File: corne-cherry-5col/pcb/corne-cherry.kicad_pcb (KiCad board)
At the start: 2 copper layers, 237.5 x 105.6 mm, 152 parts, among them J1 MJ-4PP-9, J2 OLED, J3 MJ-4PP-9, J4 OLED, SW10 SW_PUSH, SW11 SW_PUSH, SW12 SW_PUSH, SW14 SW_PUSH, SW15 SW_PUSH, SW16 SW_PUSH, SW17 SW_PUSH, SW18 SW_PUSH, SW19 SW_PUSH, SW2 SW_PUSH, SW20 SW_PUSH, SW21 SW_PUSH, SW23 SW_PUSH, SW24 SW_PUSH, SW25 SW_PUSH, SW26 SW_PUSH, SW27 SW_PUSH, SW29 SW_PUSH, SW3 SW_PUSH, SW30 SW_PUSH, SW31 SW_PUSH, SW32 SW_PUSH, SW33 SW_PUSH, SW35 SW_PUSH, SW36 SW_PUSH, SW37 SW_PUSH, SW38 SW_PUSH, SW39 SW_PUSH, SW4 SW_PUSH, SW40 SW_PUSH, SW41 SW_PUSH, SW42 SW_PUSH, SW5 SW_PUSH, SW6 SW_PUSH, SW8 SW_PUSH, SW9 SW_PUSH, U1 ProMicro, U2 ProMicro

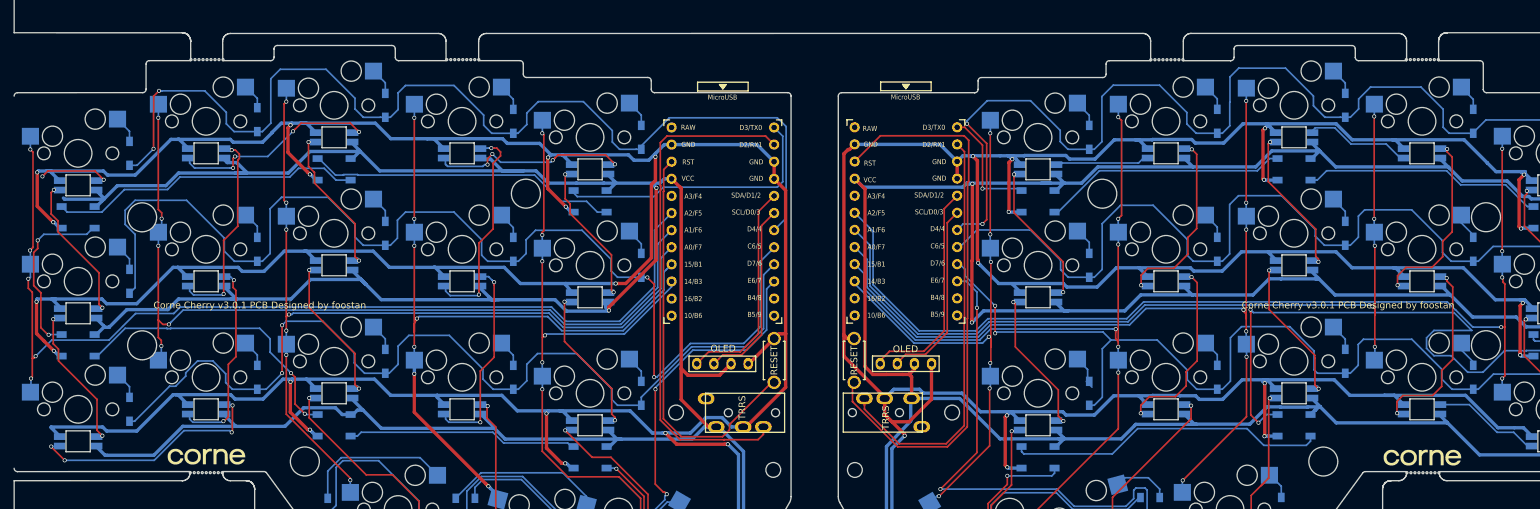
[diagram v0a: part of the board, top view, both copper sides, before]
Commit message: minor fixes to 5col
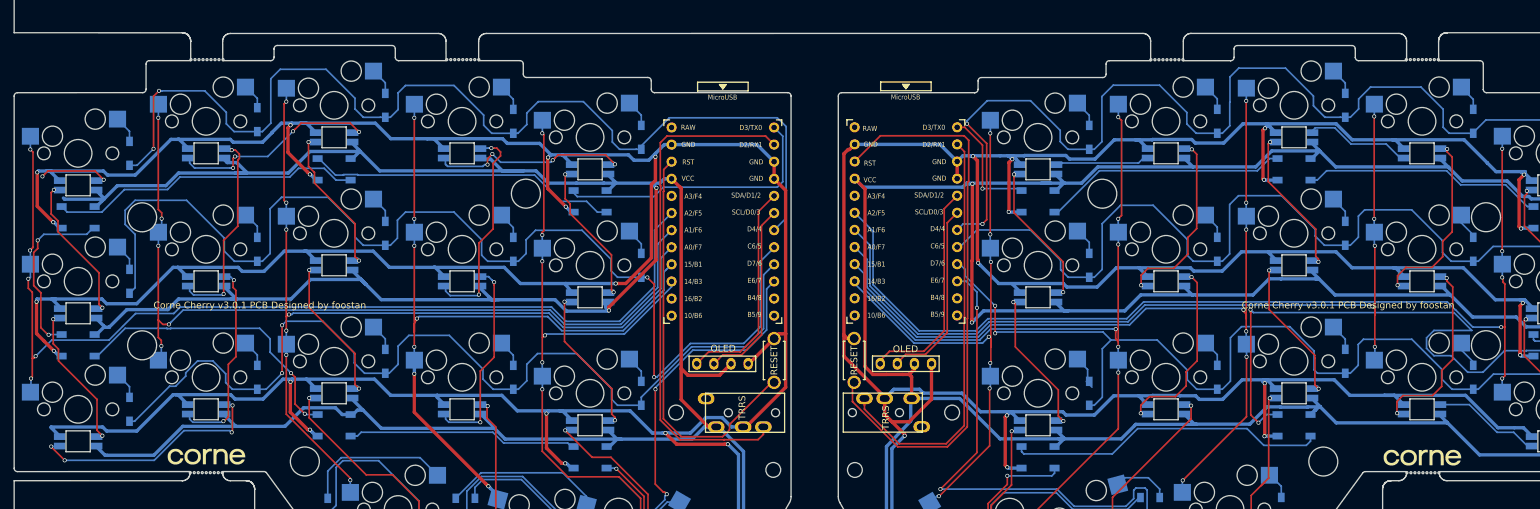
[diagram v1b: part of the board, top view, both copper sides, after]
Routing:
- net col1_r: track 151.9 -> 150.1 mm
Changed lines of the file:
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@@
   (gr_line (start 55.7125 83.245) (end 55.7175 83.020309)
     (stroke (width 0.2) (type solid)) (layer "Edge.Cuts"))
-  (gr_line (start 93.7275 22.020252) (end 93.7125 19.1227)
-    (stroke (width 0.2) (type solid)) (layer "Edge.Cuts"))
   (gr_line (start 93.7125 19.1227) (end 93.7125 19.1169)
     (stroke (width 0.2) (type solid)) (layer "Edge.Cuts"))
@@
   (gr_line (start 67.688301 22.018729) (end 60.5775 22.018729)
     (stroke (width 0.2) (type solid)) (layer "Edge.Cuts"))
-  (gr_line (start 49.189499 22.519109) (end 49.189499 26.268145)
-    (stroke (width 0.2) (type solid)) (layer "Edge.Cuts"))
   (gr_curve (pts (xy 124.190287 25.020242) (xy 124.190346 24.744107) (xy 123.966569 24.520195) (xy 123.690423 24.520121))
     (stroke (width 0.2) (type solid)) (layer "Edge.Cuts"))
@@
   (gr_line (start 104.688444 22.018729) (end 98.5675 22.018729)
     (stroke (width 0.2) (type solid)) (layer "Edge.Cuts"))
-  (gr_line (start 86.189642 21.51835) (end 86.189642 20.268671)
-    (stroke (width 0.2) (type solid)) (layer "Edge.Cuts"))
-  (gr_line (start 85.689263 19.768292) (end 68.68906 19.768292)
-    (stroke (width 0.2) (type solid)) (layer "Edge.Cuts"))
   (gr_line (start 144.939784 27.268904) (end 144.939784 86.742945)
     (stroke (width 0.2) (type solid)) (layer "Edge.Cuts"))
@@
   (gr_line (start 29.6075 84.38) (end 54.5748 84.385)
     (stroke (width 0.2) (type default)) (layer "Edge.Cuts"))
+  (gr_line (start 86.190406 20.270194) (end 86.190406 21.520126)
+    (stroke (width 0.2) (type default)) (layer "Edge.Cuts"))
   (gr_line (start 266.607378 83.029873) (end 241.1775 83.027309)
     (stroke (width 0.2) (type default)) (layer "Edge.Cuts"))
   (gr_line (start 267.1075 84.38) (end 267.1075 117.63)
     (stroke (width 0.2) (type default)) (layer "Edge.Cuts"))
+  (gr_line (start 93.7125 19.1169) (end 93.7275 22.020252)
+    (stroke (width 0.2) (type default)) (layer "Edge.Cuts"))
   (gr_line (start 247.204616 22.028252) (end 241.0775 22.028252)
     (stroke (width 0.2) (type solid)) (layer "Edge.Cuts"))
@@
   (gr_line (start 267.1075 12.03) (end 267.1075 17.88)
     (stroke (width 0.2) (type default)) (layer "Edge.Cuts"))
+  (gr_line (start 85.690533 19.770068) (end 68.69033 19.770068)
+    (stroke (width 0.2) (type default)) (layer "Edge.Cuts"))
   (gr_line (start 230.204661 83.028073) (end 236.3275 83.028073)
     (stroke (width 0.2) (type solid)) (layer "Edge.Cuts"))
@@
   (gr_line (start 29.6075 117.63) (end 29.6075 84.38)
     (stroke (width 0.2) (type default)) (layer "Edge.Cuts"))
+  (gr_line (start 29.607373 27.279868) (end 29.6075 82.53)
+    (stroke (width 0.2) (type default)) (layer "Edge.Cuts"))
   (gr_line (start 29.6075 117.63) (end 267.1075 117.63)
+    (stroke (width 0.2) (type default)) (layer "Edge.Cuts"))
+  (gr_line (start 49.190511 22.520126) (end 49.190511 26.270179)
     (stroke (width 0.2) (type default)) (layer "Edge.Cuts"))
   (gr_line (start 248.204611 26.778301) (end 266.607373 26.780132)
@@
   (segment (start 194.781216 60.329976) (end 197.273203 57.837989) (width 0.254) (layer "B.Cu") (net 67))
   (segment (start 250.5295 54.183) (end 250.5075 54.205) (width 0.25) (layer "B.Cu") (net 67))
-  (segment (start 248.64751 64.10001) (end 249.9975 64.10001) (width 0.25) (layer "B.Cu") (net 67))
   (segment (start 172.365167 62.128955) (end 174.164145 60.329977) (width 0.254) (layer "B.Cu") (net 67))
   (segment (start 250.5075 71.213) (end 250.5295 71.235) (width 0.25) (layer "B.Cu") (net 67))
@@
   (segment (start 243.496865 58.970125) (end 243.6075 59.04) (width 0.254) (layer "B.Cu") (net 67))
   (segment (start 243.6075 59.04) (end 246.1475 61.58) (width 0.254) (layer "B.Cu") (net 67))
-  (segment (start 248.3775 63.83) (end 248.64751 64.10001) (width 0.25) (layer "B.Cu") (net 67))
   (segment (start 154.3839 44.613) (end 157.113491 47.342591) (width 0.254) (layer "B.Cu") (net 67))
   (segment (start 250.5075 50.305) (end 250.5075 52.213) (width 0.25) (layer "B.Cu") (net 67))
